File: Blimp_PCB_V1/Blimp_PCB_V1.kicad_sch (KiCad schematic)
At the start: 16 parts, among them J1 S8B-PH-K-S

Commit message: PCBv1.2
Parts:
- removed C1: 100uF, Capacitor_SMD:C_0603_1608Metric_Pad1.08x0.95mm_HandSolder, symbol Device:C
- removed P5: ~, PINS:PWM, symbol PWM:PWM
- removed P7: ~, PINS:Shorting Pins, symbol Shorting Pints:Shorting_Pins
- added P5: ~, PINS:Latching Pins, symbol Shorting Pints:Shorting_Pins
- P6: footprint PINS:Shorting Pins -> PINS:Latching Pins
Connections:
- net +5V: no longer U3.1
- net BV: now also P5.1
- net GND: now also P5.2
- net at P8.2: now also U3.2; no longer P6.2
- net at J1.8: now also P8.4
- net at P6.1: now also P8.23; no longer U3.2
- net at P2.1 (PWM): no longer P8.4
- net at P8.22: now also P6.2
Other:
- note added: "GND"
- note added: "IMU"
- note added: "POWER"
- note added: "SIGNAL"
- moved on the sheet: B1, C2, C3, J1, P1, P2, P3, P4, P8, P9, U2, U3

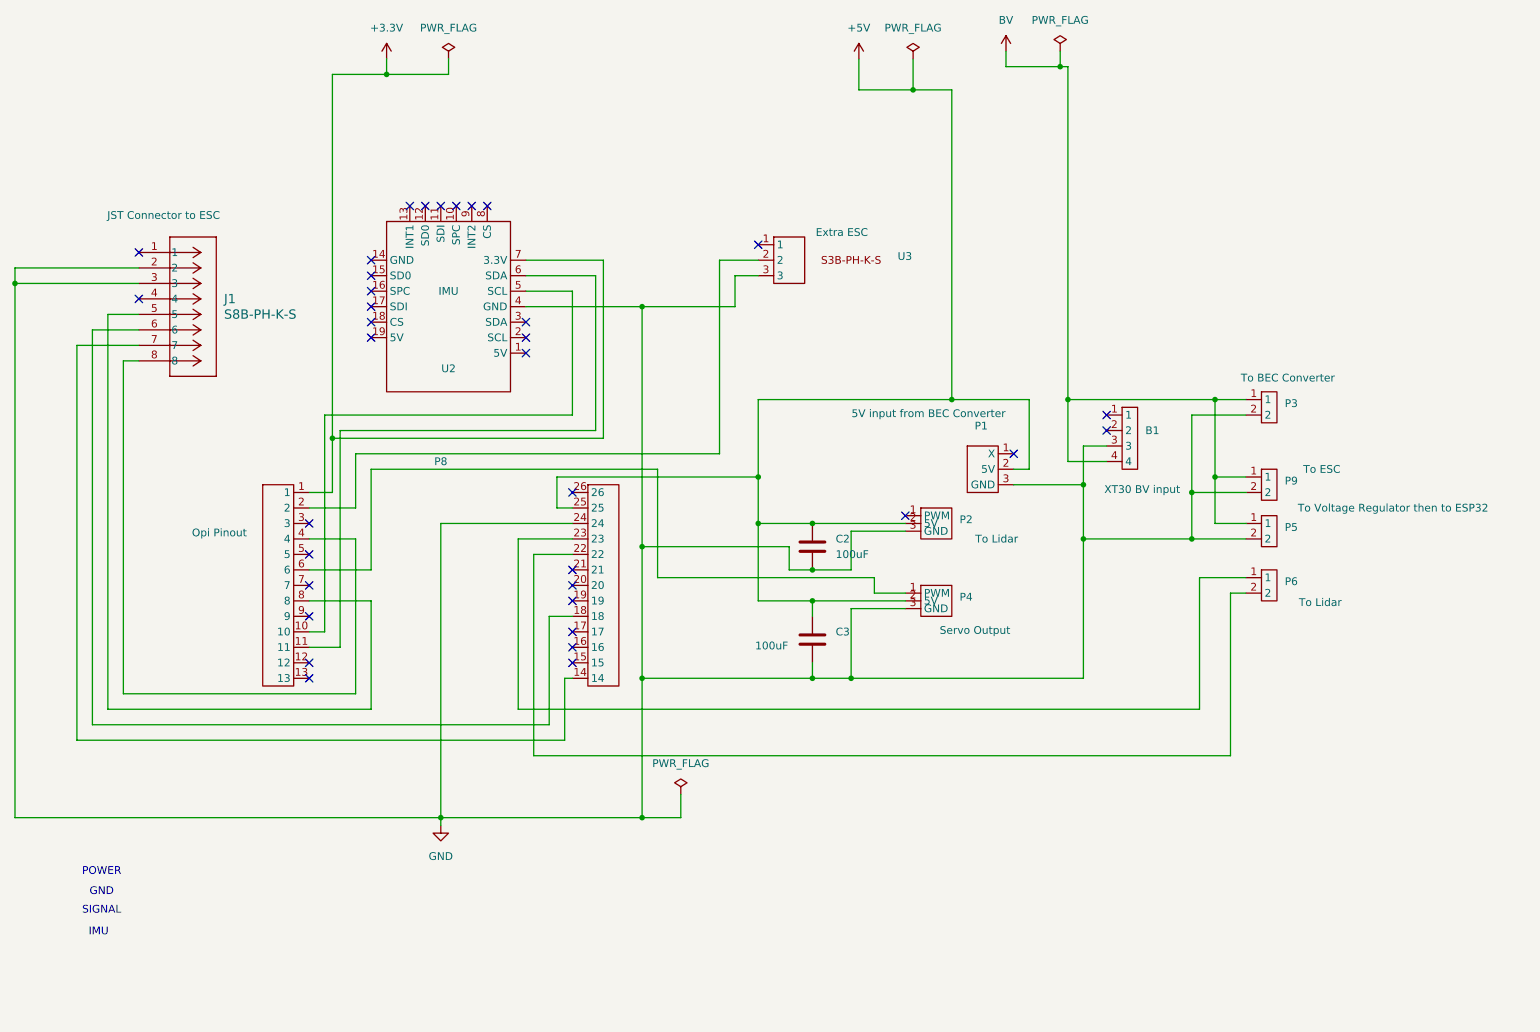
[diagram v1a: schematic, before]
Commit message: PCBv1 modified schematic
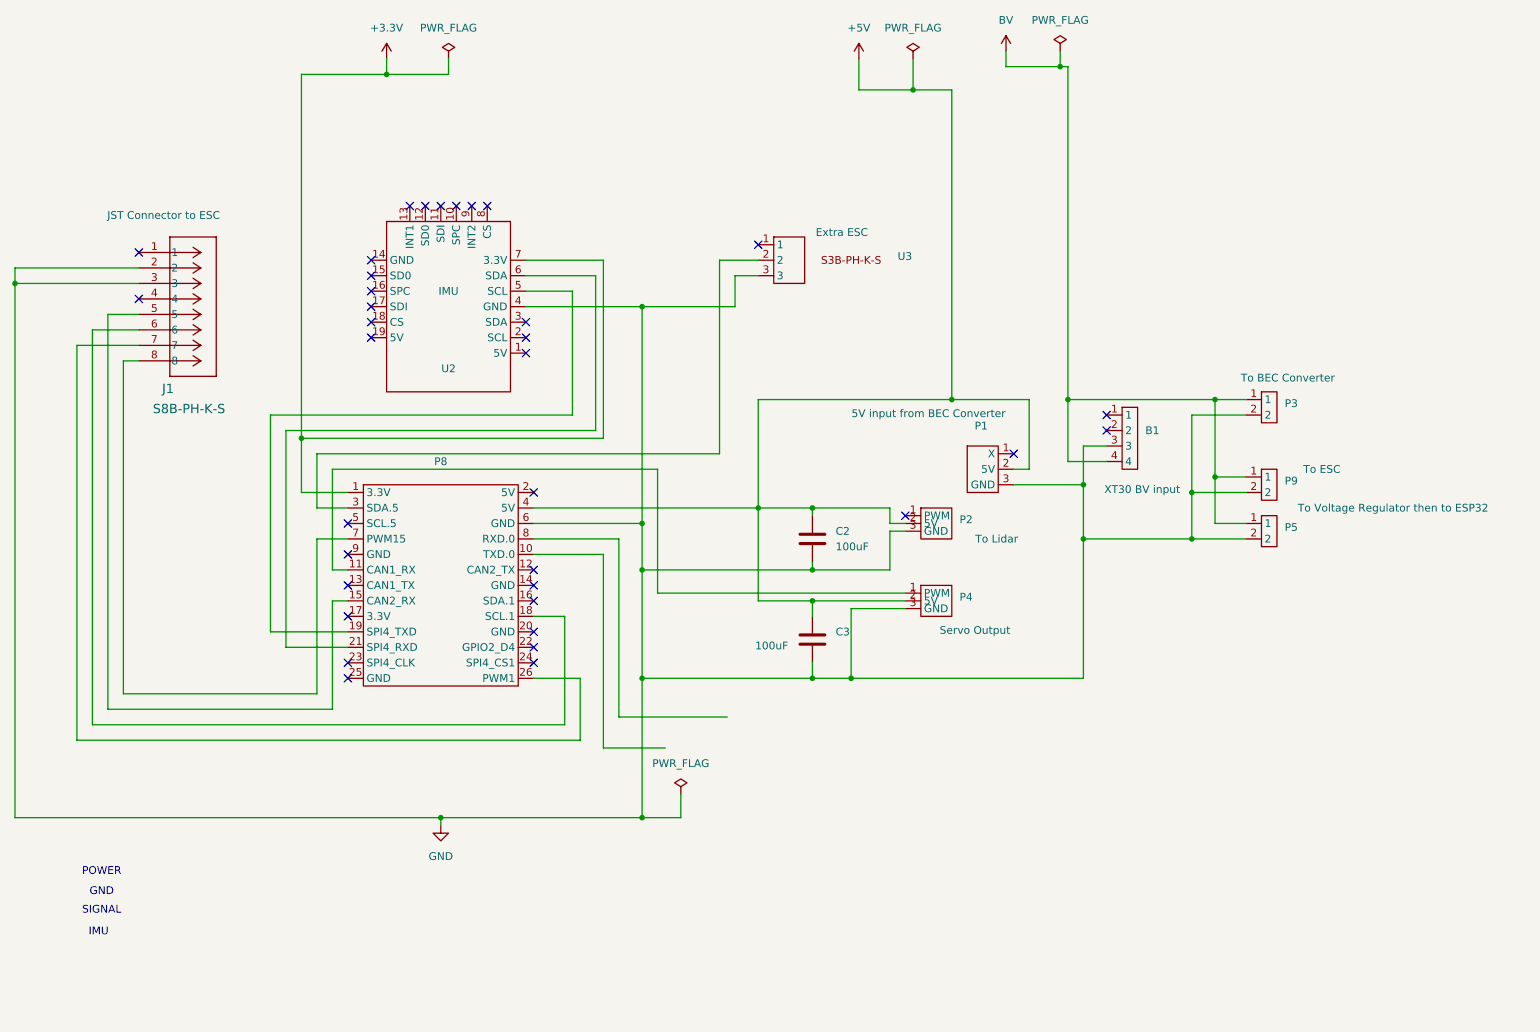
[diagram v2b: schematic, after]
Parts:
- removed P6: ~, PINS:Latching Pins, symbol Shorting Pints:Shorting_Pins
- P5: footprint PINS:Latching Pins -> Pins:Shorting Pins
- P8: footprint PINS:26-PIN Female -> Blimp Library:Orange_Pi_5B; symbol Female Pins:Female_Pins -> Orange_Pi_Symbol:Female_Pins
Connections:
- net +5V: now also P8.4 (5V); no longer P8.25
- net GND: now also P8.6 (GND); no longer P8.24
- net at J1.5: now also P8.15 (CAN2_RX); no longer P8.8
- net at J1.7: now also P8.26 (PWM1); no longer P8.14
- net at J1.8: now also P8.7 (PWM15); no longer P8.4
- net at U3.2: now also P8.3 (SDA.5); no longer P8.2
- net at P4.1 (PWM): now also P8.11 (CAN1_RX); no longer P8.6
- net at U2.5 (SCL): now also P8.19 (SPI4_TXD); no longer P8.10
- net at U2.6 (SDA): now also P8.21 (SPI4_RXD); no longer P8.11
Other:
- moved on the sheet: C2

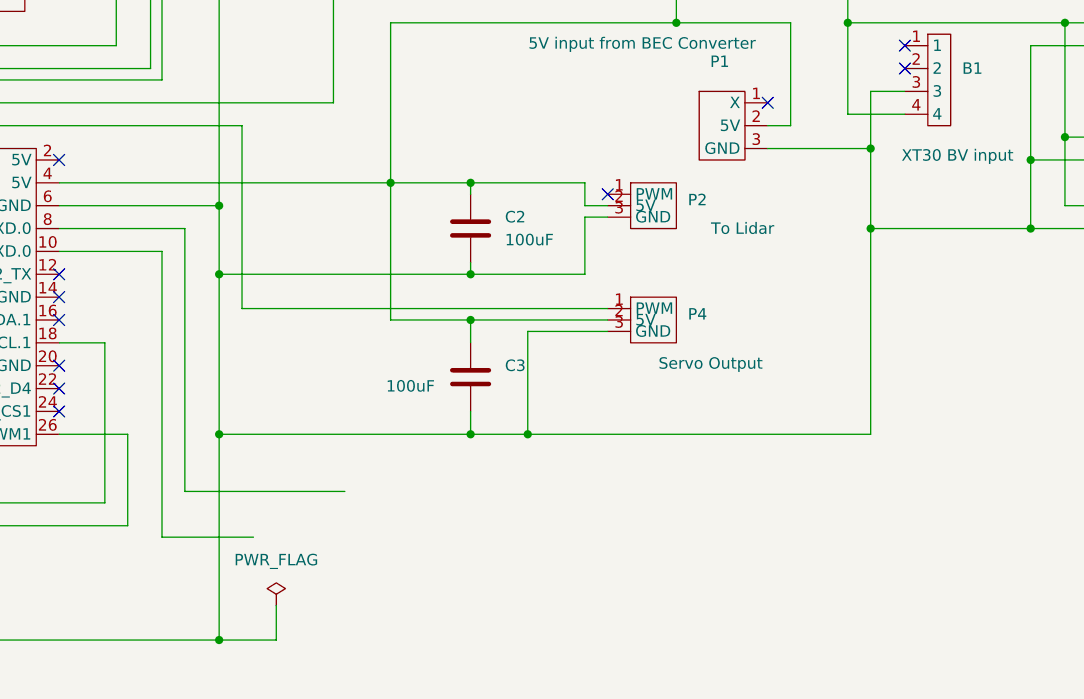
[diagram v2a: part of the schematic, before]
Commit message: Added proper JST Connector for Lidar, Footprint and Symbol
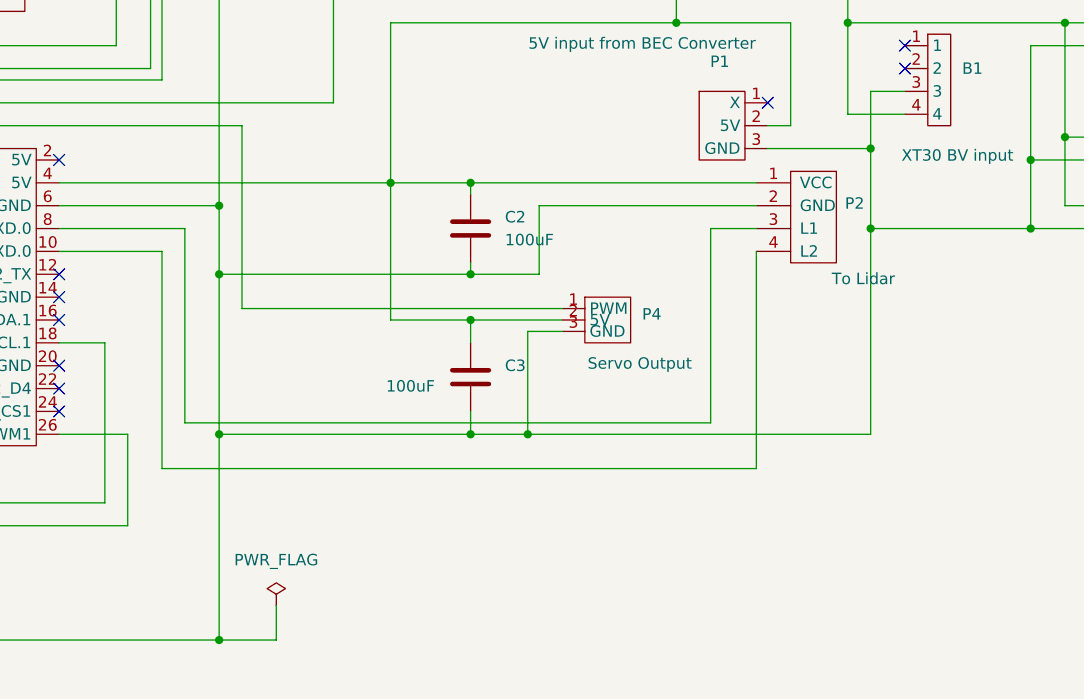
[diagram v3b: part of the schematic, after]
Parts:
- removed P2: ~, PINS:PWM, symbol PWM:PWM
- added P2: ~, symbol Connector:Conn_01x04_Pin
- J1: footprint JST Connector:S8B-PH-K-S -> JST Connector:JST_SH_SM08B-SRSS-TB_1x08-1MP_P1.00mm_Horizontal
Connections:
- net +5V: now also P2.1 (VCC)
- net GND: now also P2.2 (GND)
- net at P8.10 (TXD.0): now also P2.4 (L2)
- net at P8.8 (RXD.0): now also P2.3 (L1)
- no-connect marks 35 -> 34
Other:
- moved on the sheet: P4
